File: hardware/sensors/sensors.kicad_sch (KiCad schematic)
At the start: 51 parts, among them J1 SWITCHES-SENSORS, J6 IRDA, SW1 SW_Push, SW2 SW_Push, SW3 SW_Push, SW4 SW_Push, U1 EKMC1604111, U2 DS18B20, U3 BME680, U4 BME280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

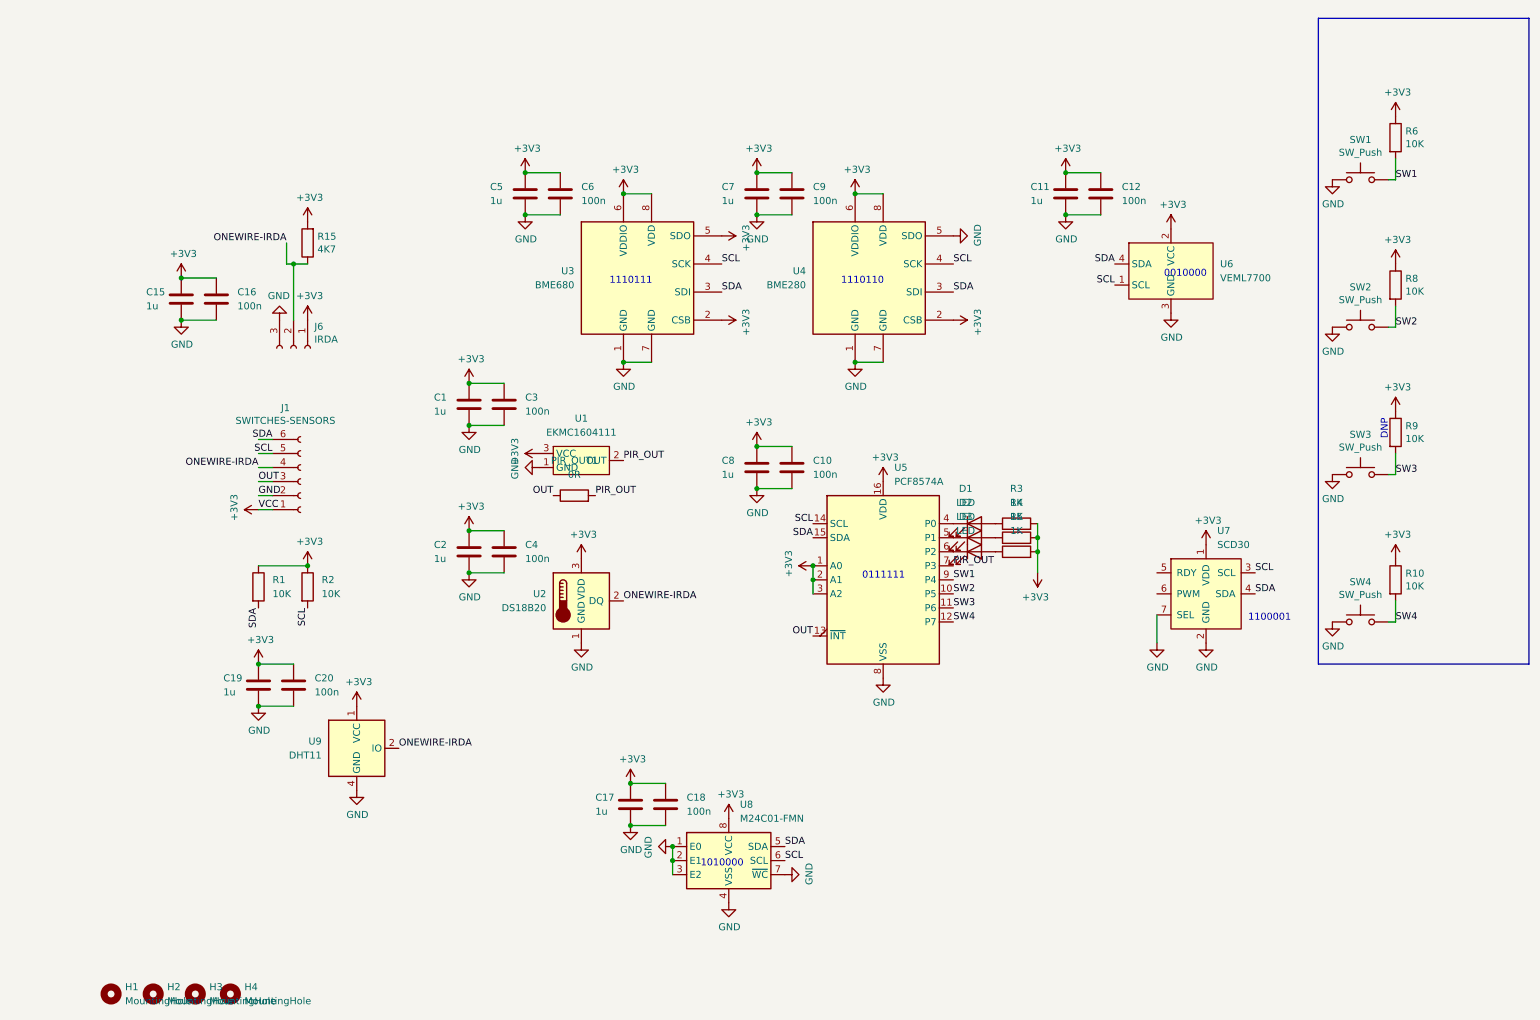
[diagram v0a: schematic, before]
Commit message: feat: change PCB debug to EN/BOOT0
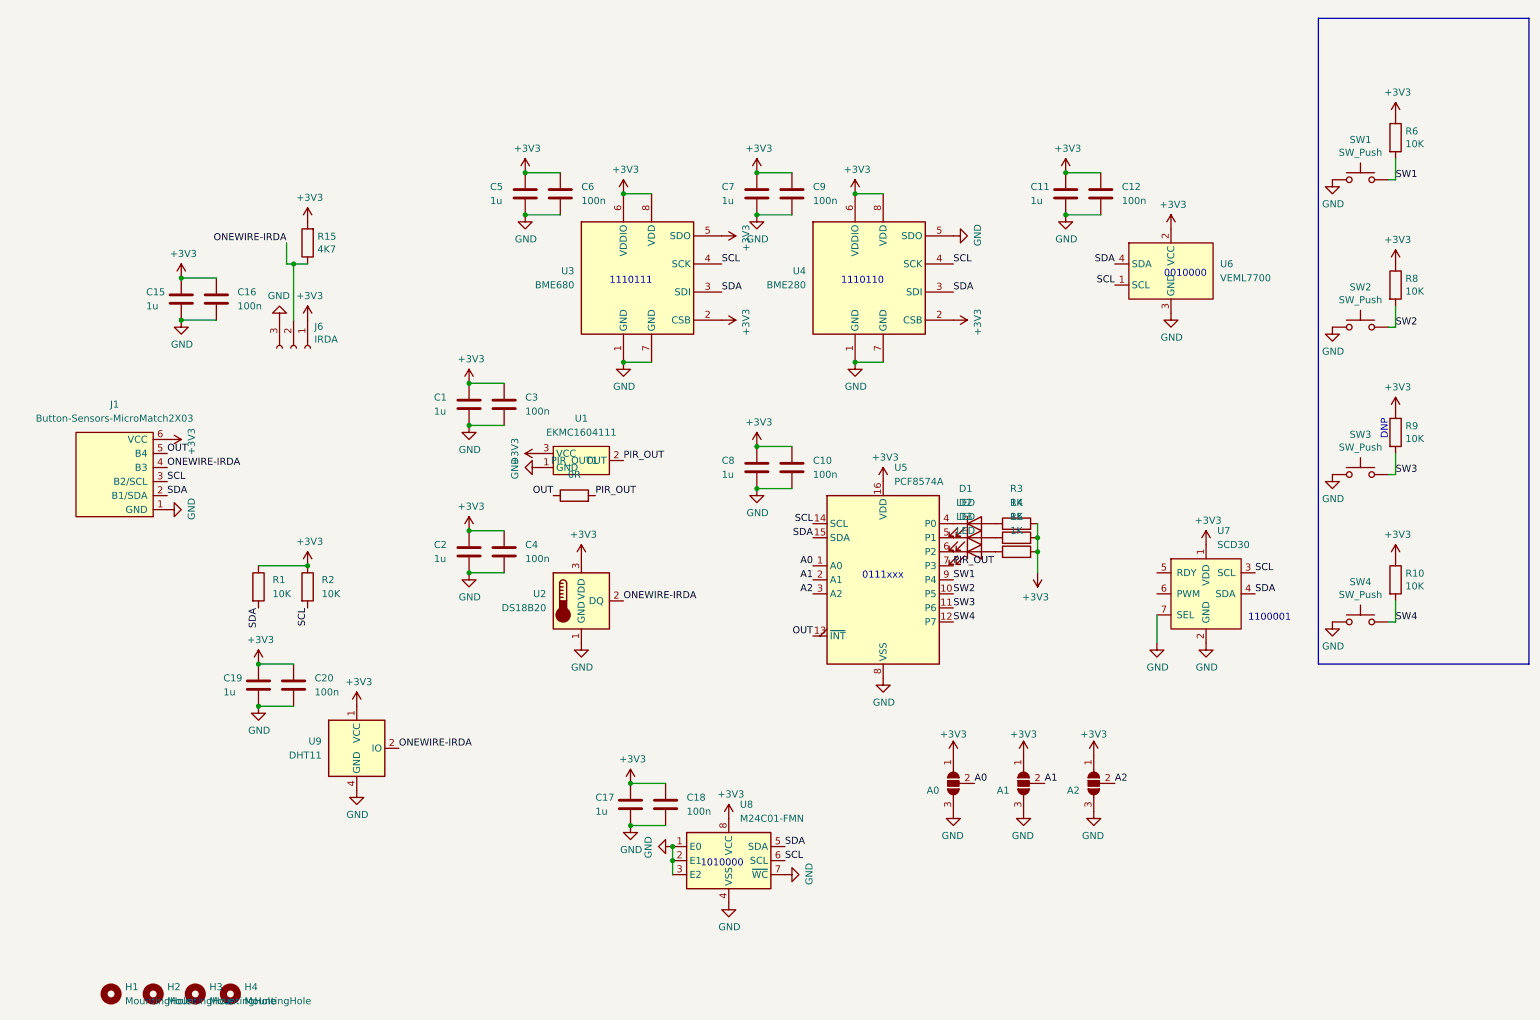
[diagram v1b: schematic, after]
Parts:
- removed J1: SWITCHES-SENSORS, awesome:02x03MicroMatch, symbol Connector:Conn_01x06_Female
- added A0, A1, A2: SolderJumper_3_Open, Jumper:SolderJumper-3_P1.3mm_Open_RoundedPad1.0x1.5mm, symbol Jumper:SolderJumper_3_Open
- added J1: Button-Sensors-MicroMatch2X03, awesome:02x03MicroMatch, symbol awesome:Button-Sensors-MicroMatch2X03
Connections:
- net +3V3: now also A0.1 (A), A1.1 (A), A2.1 (A), J1.6 (VCC); no longer U5.1 (A0), U5.2 (A1), U5.3 (A2)
- net GND: now also A0.3 (B), A1.3 (B), A2.3 (B), J1.1 (GND)
- net ONEWIRE-IRDA: now also J1.4 (B3)
- net OUT: now also J1.5 (B4)
- net SCL: now also J1.3 (B2/SCL)
- net SDA: now also J1.2 (B1/SDA)
- new net A0: A0.2 (C), U5.1 (A0)
- new net A1: A1.2 (C), U5.2 (A1)
- new net A2: A2.2 (C), U5.3 (A2)
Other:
- note added: "0111xxx"
- note removed: "0111111"

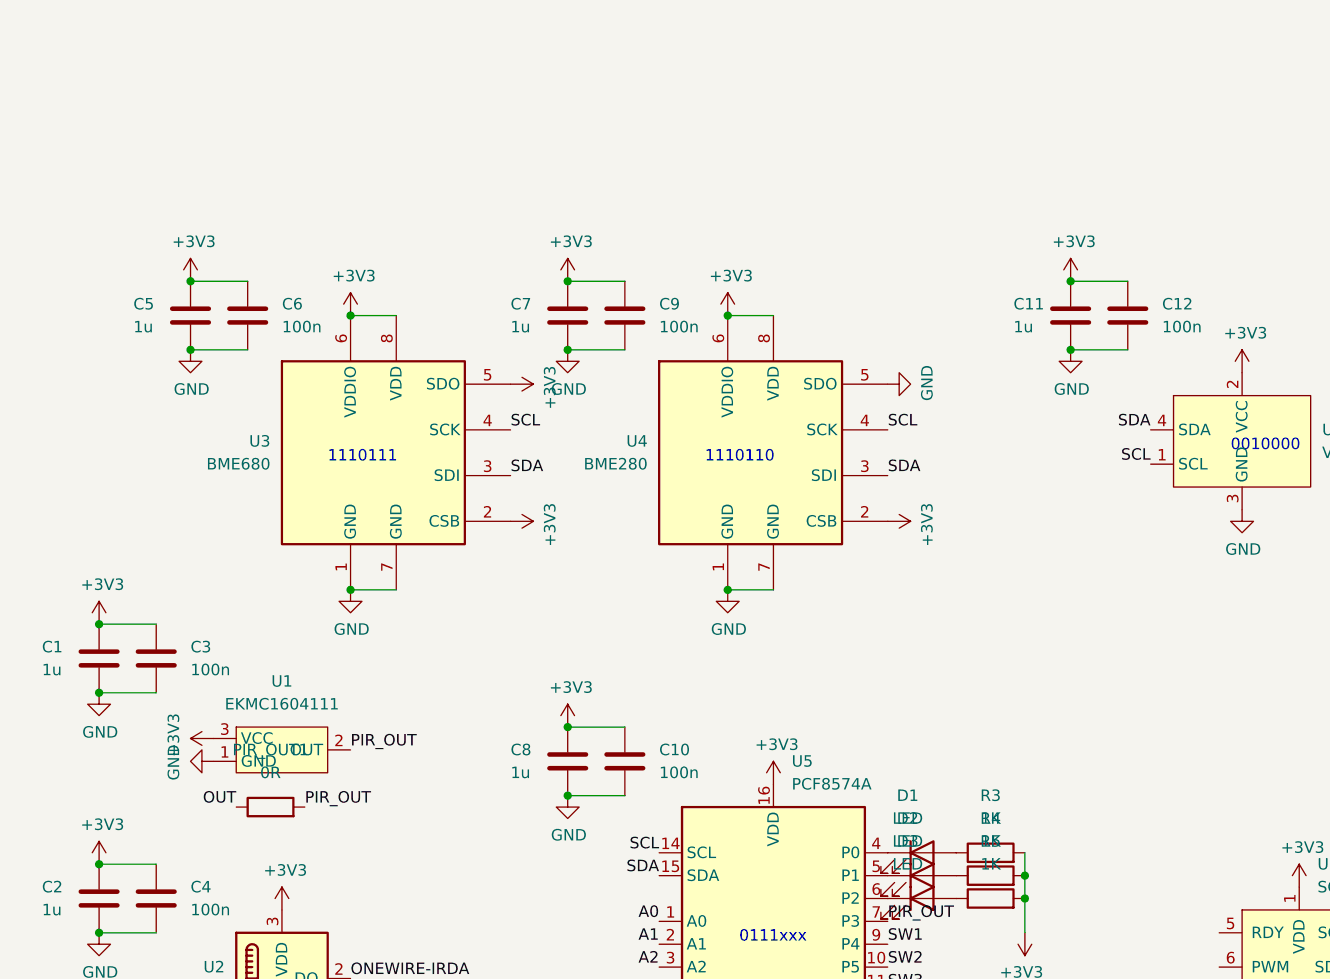
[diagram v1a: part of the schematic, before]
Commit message: feat: Add fab export options for all pcbs
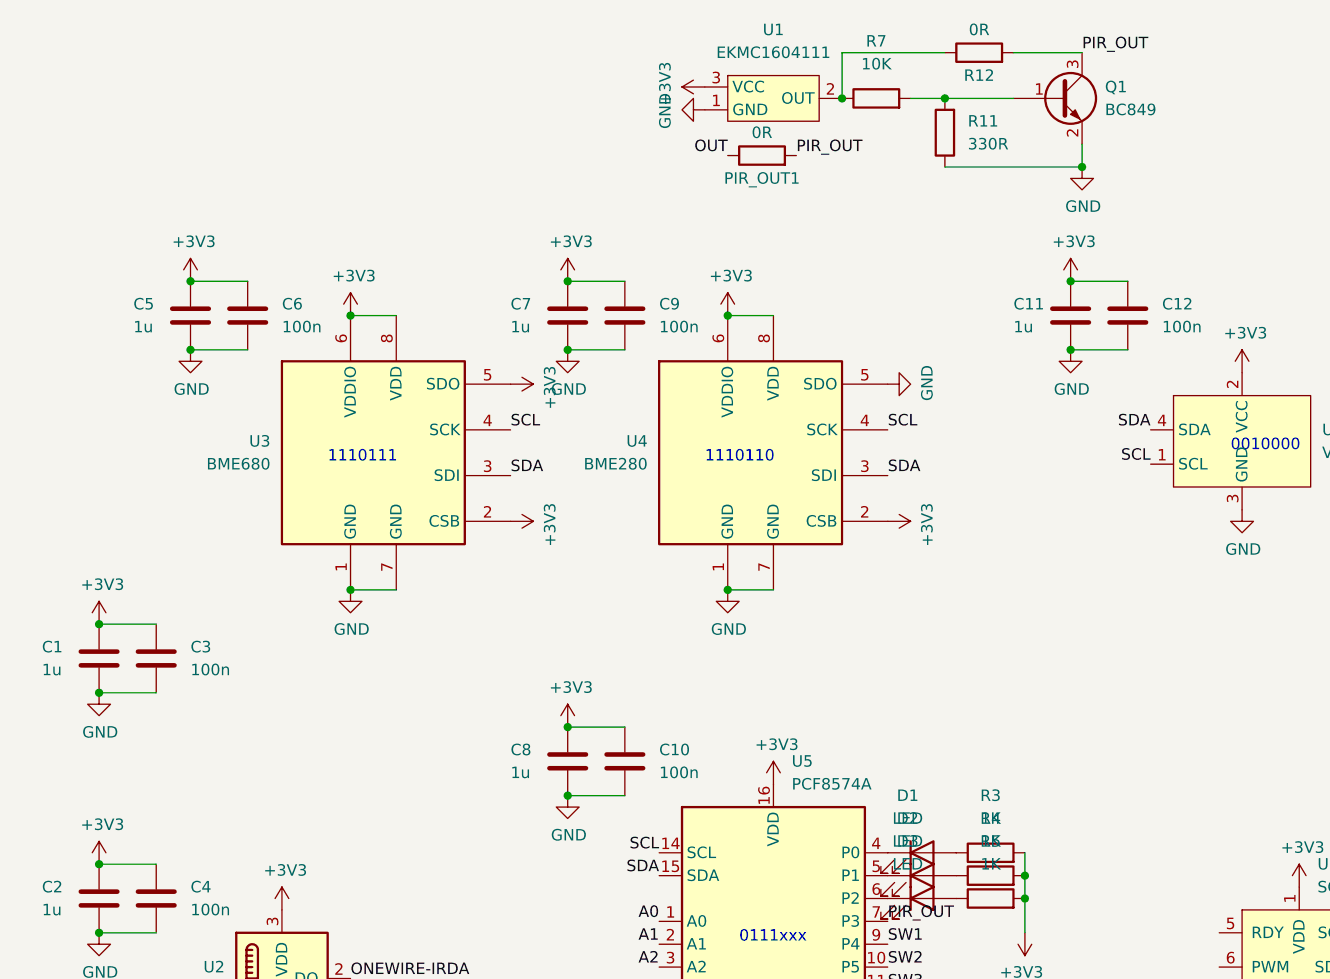
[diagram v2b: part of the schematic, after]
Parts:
- added Q1: BC849, Package_TO_SOT_SMD:SOT-23, symbol Transistor_BJT:BC849
- added R11: 330R, Resistor_SMD:R_0603_1608Metric_Pad0.98x0.95mm_HandSolder, symbol Device:R
- added R12: 0R, Jumper:SolderJumper-2_P1.3mm_Open_RoundedPad1.0x1.5mm, symbol Device:R
- added R7: 10K, Resistor_SMD:R_0603_1608Metric_Pad0.98x0.95mm_HandSolder, symbol Device:R
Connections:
- net GND: now also Q1.2 (E), R11.1
- net PIR_OUT: now also Q1.3 (C), R12.2; no longer U1.2 (OUT)
- new net: Q1.1 (B), R11.2, R7.2
- new net: R12.1, R7.1, U1.2 (OUT)
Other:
- moved on the sheet: PIR_OUT1, U1
